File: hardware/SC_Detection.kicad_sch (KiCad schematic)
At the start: 86 parts, among them U15 LT1678CS8#PBF, U16 LT1678CS8#PBF, U17 LM211DRG4, U18 LM211DRG4, U19 LM211DRG4, U20 LM211DRG4

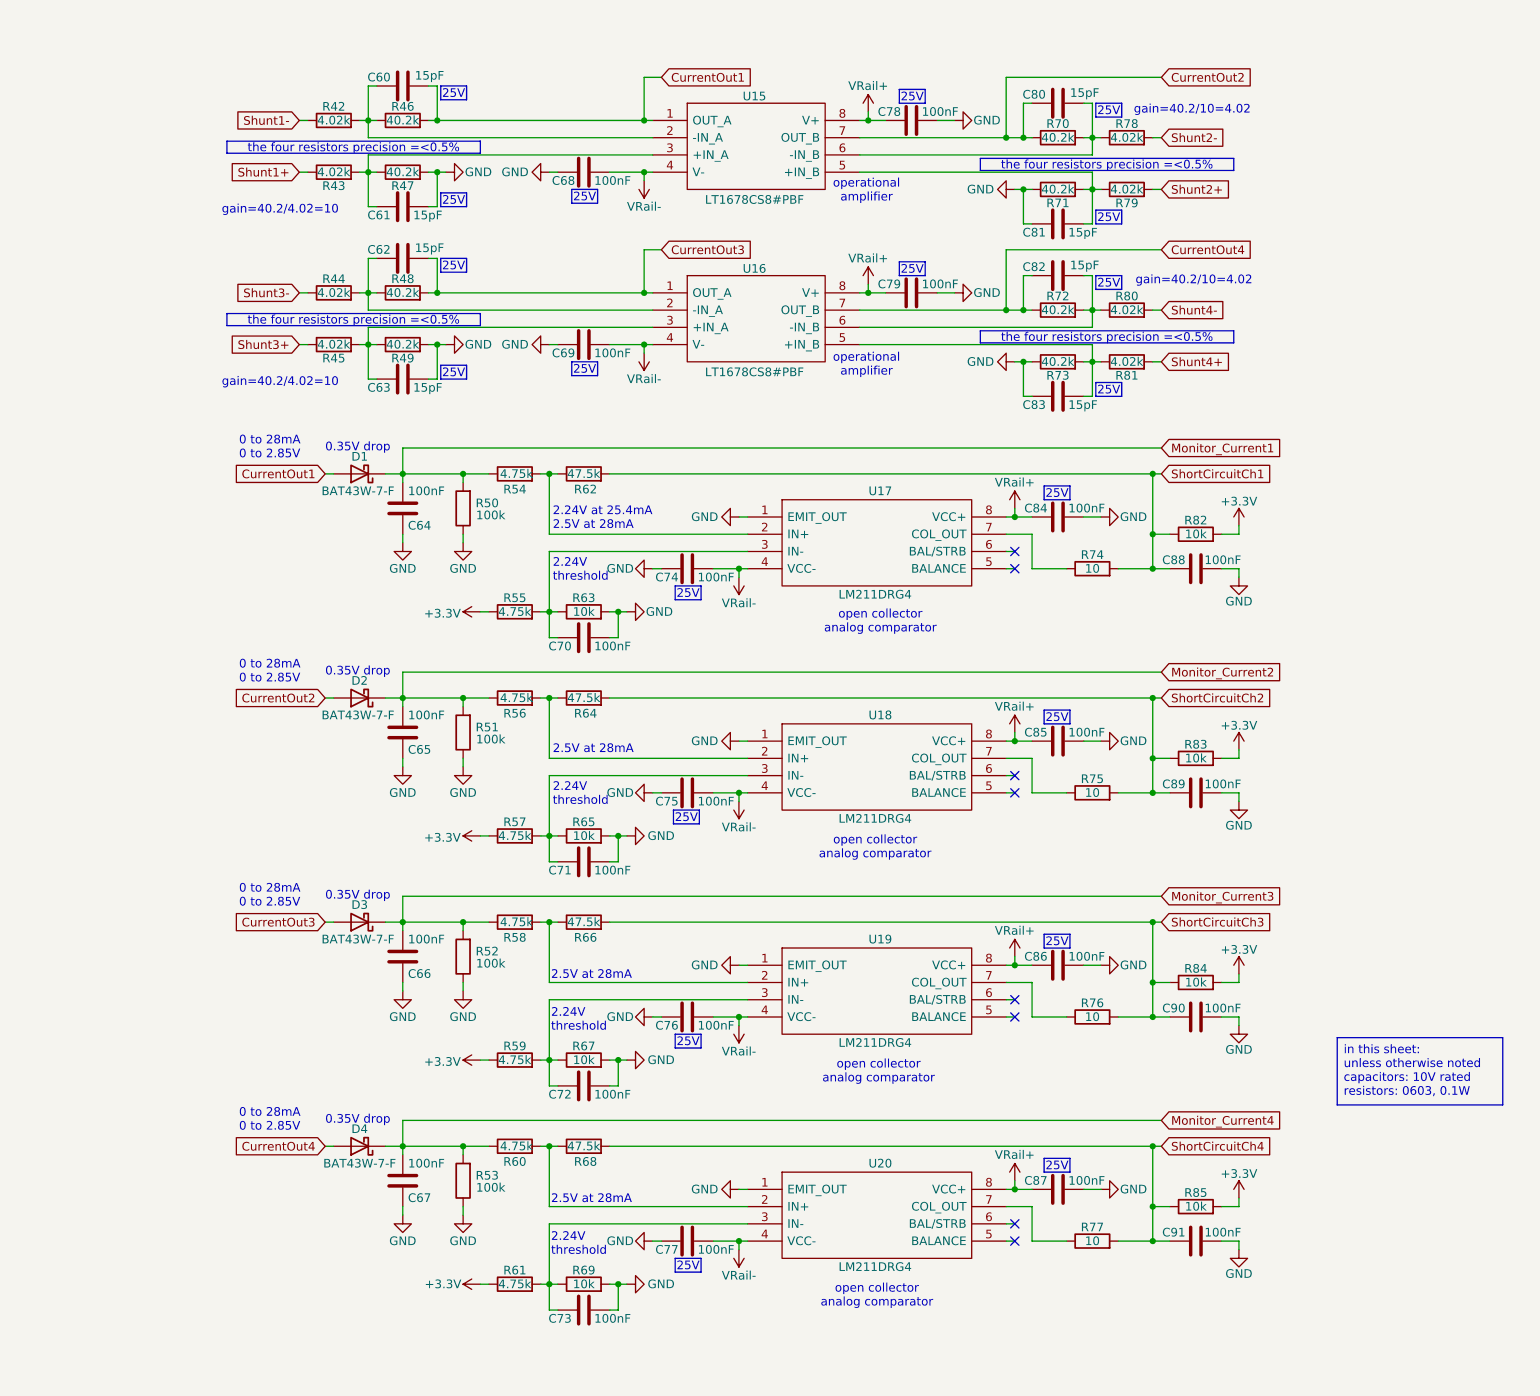
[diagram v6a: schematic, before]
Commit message: BOM for all capacitors and resistors is added correctly to the schematic
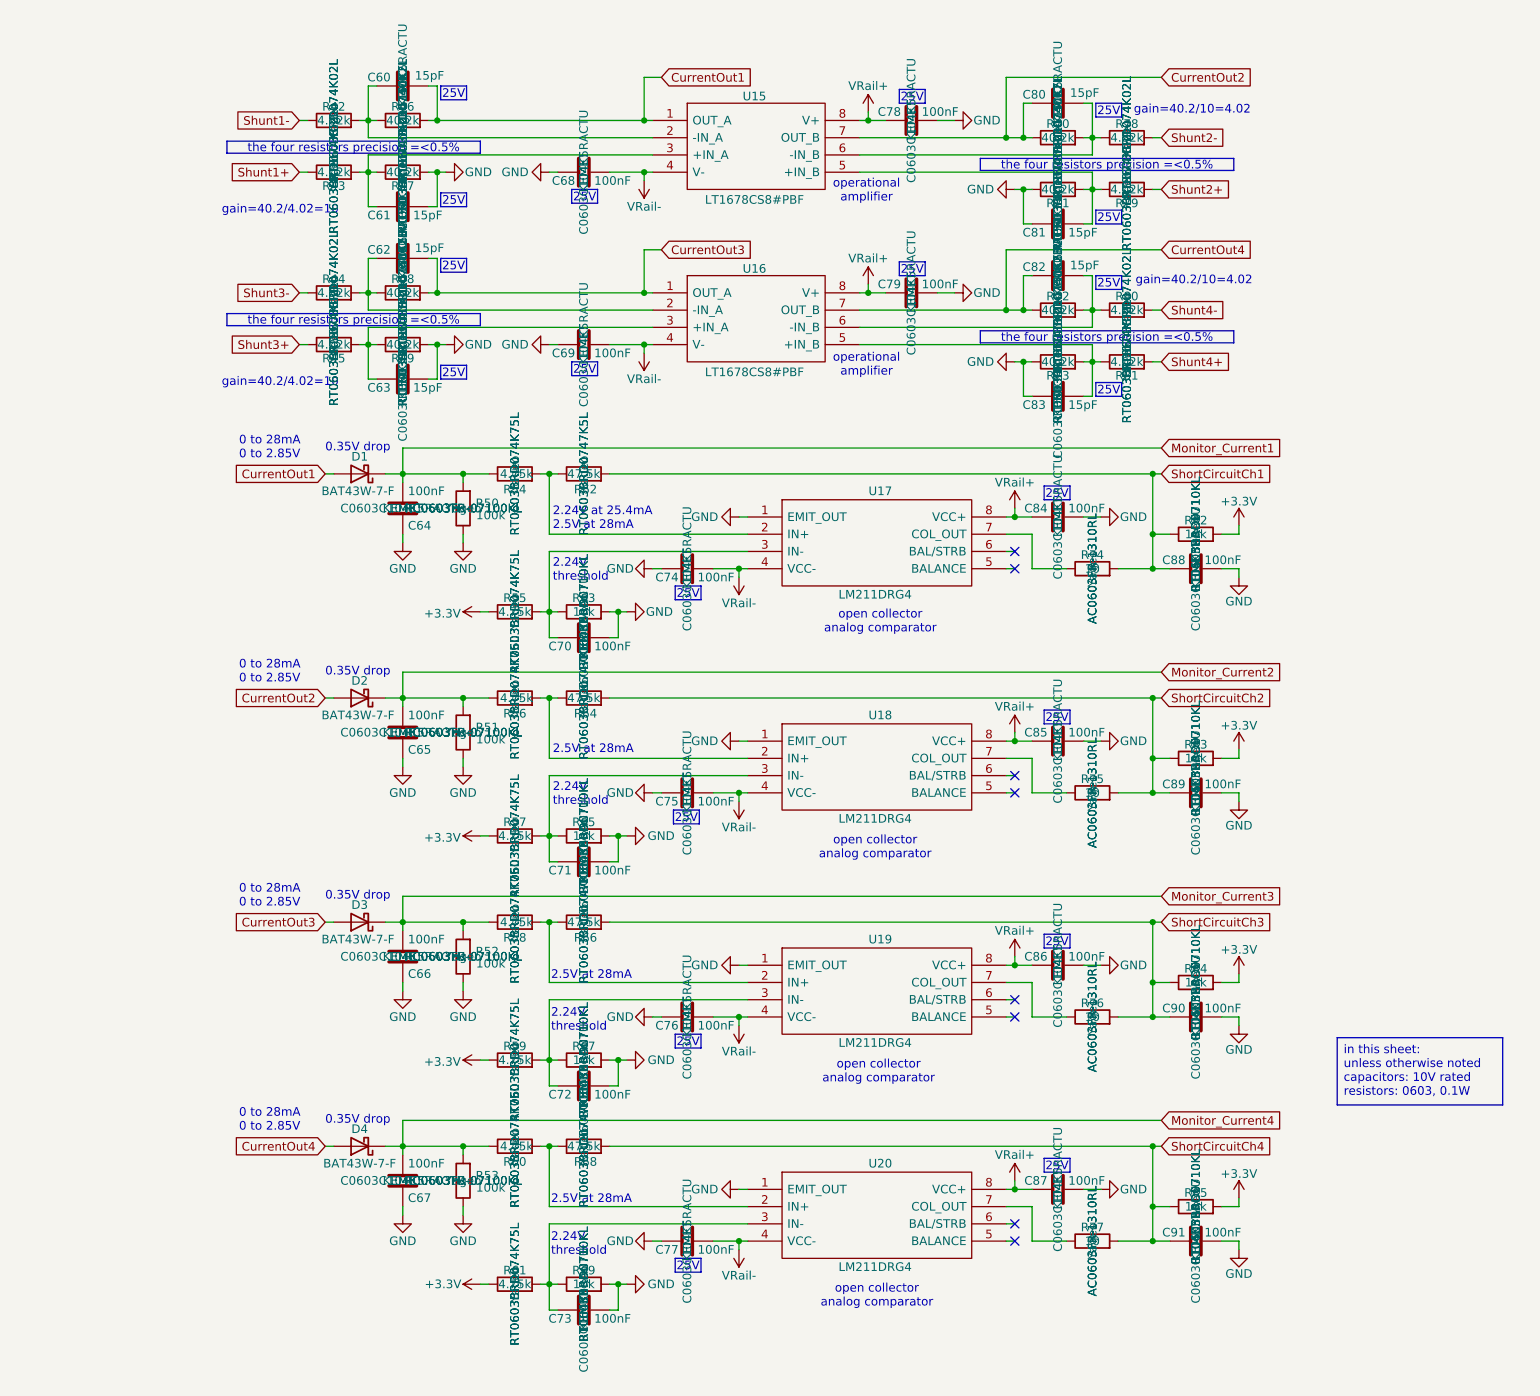
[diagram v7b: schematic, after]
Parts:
- C60, C61, C62, C63, C80, C81, C82, C83: Link https://www.digikey.com/en/products/detail/walsin-technolog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 -> https://www.digikey.com/en/products/detail/kemet/C0603C150K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; MPN (none) -> C0603C150K5RACTU; Manufacturer Walson Technology Corporation -> KEMET; Manufacturer Number 0402B104K160CT -> (none); Manufacturer_Name (none) -> KEMET; Manufacturer_Part_Number (none) -> C0603C150K5RACTU; Rated Voltage 16V -> 50V
- C64, C65, C66, C67, C68, C69, C70, C71, C72, C73, C74, C75, C76, C77, C78, C79, C84, C85, C86, C87, C88, C89, C90, C91: Link https://www.digikey.com/en/products/detail/walsin-technolog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 -> https://www.digikey.com/en/products/detail/kemet/C0603C104K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; MPN (none) -> C0603C104K5RACTU; Manufacturer Walson Technology Corporation -> KEMET; Manufacturer Number 0402B104K160CT -> (none); Manufacturer_Name (none) -> KEMET; Manufacturer_Part_Number (none) -> C0603C104K5RACTU; Rated Voltage 16V -> 50V
- R42, R43, R44, R45, R78, R79, R80, R81: Link https://www.digikey.com/en/products/detail/yageo/RT0402BRD0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 -> https://www.digikey.com/en/products/detail/yageo/RT0603BRD0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; MPN (none) -> RT0603BRD074K02L; Manufacturer_Name (none) -> Yageo; Manufacturer_Part_Number (none) -> RT0603BRD074K02L; Tolerance 1% -> 0.1%
- R46, R47, R48, R49, R70, R71, R72, R73: Link https://www.digikey.com/en/products/detail/yageo/RT0402BRD0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 -> https://www.digikey.com/en/products/detail/yageo/RT0603BRD0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; MPN (none) -> RT0603BRD0740K2L; Manufacturer_Name (none) -> Yageo; Manufacturer_Part_Number (none) -> RT0603BRD0740K2L; Tolerance 1% -> 0.1%
- R50, R51, R52, R53: Link https://www.digikey.com/en/products/detail/yageo/RT0402BRD0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 -> https://www.digikey.com/en/products/detail/yageo/RC0603FR-0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; MPN (none) -> RC0603FR-07100KL; Manufacturer_Name (none) -> Yageo; Manufacturer_Part_Number (none) -> RC0603FR-07100KL
- R54, R55, R56, R57, R58, R59, R60, R61: Link https://www.digikey.com/en/products/detail/yageo/RT0402BRD0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 -> https://www.digikey.com/en/products/detail/yageo/RT0603BRD0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; MPN (none) -> RT0603BRD074K75L; Manufacturer_Name (none) -> Yageo; Manufacturer_Part_Number (none) -> RT0603BRD074K75L; Tolerance 1% -> 0.1%
- R62, R64, R66, R68: Link https://www.digikey.com/en/products/detail/yageo/RT0402BRD0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 -> https://www.digikey.com/en/products/detail/yageo/RT0603BRD0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; MPN (none) -> RT0603BRD0747K5L; Manufacturer_Name (none) -> Yageo; Manufacturer_Part_Number (none) -> RT0603BRD0747K5L
- R63, R65, R67, R69, R82, R83, R84, R85: Link https://www.digikey.com/en/products/detail/yageo/RT0402BRD0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 -> https://www.digikey.com/en/products/detail/yageo/RT0603BRD0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; MPN (none) -> RT0603BRD0710KL; Manufacturer_Name (none) -> Yageo; Manufacturer_Part_Number (none) -> RT0603BRD0710KL; Tolerance 1% -> 0.1%
- R74, R75, R76, R77: Link https://www.digikey.com/en/products/detail/yageo/RT0402BRD0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 -> https://www.digikey.com/en/products/detail/yageo/AC0603FR-1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; MPN (none) -> AC0603FR-1310RL; Manufacturer_Name (none) -> Yageo; Manufacturer_Part_Number (none) -> AC0603FR-1310RL

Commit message: Not necessary text is hidden + BOM on schematic
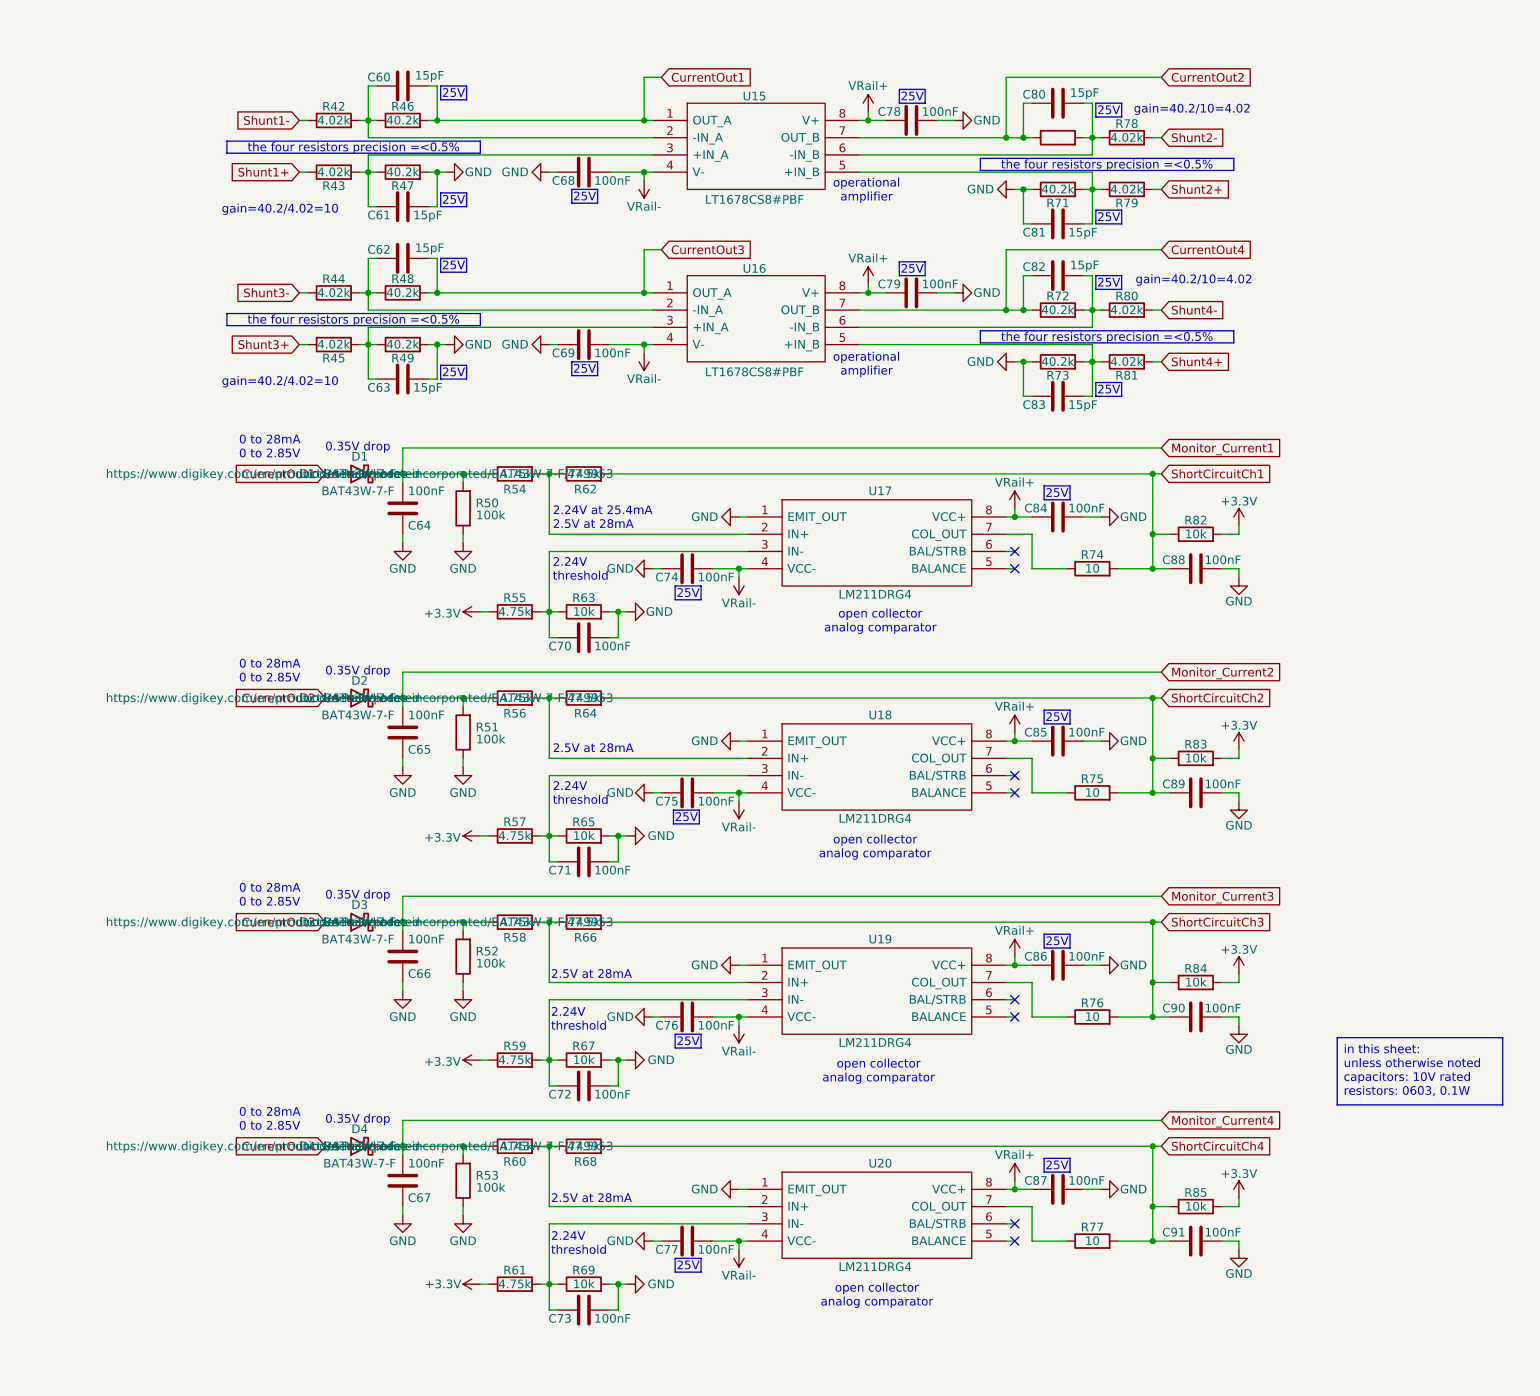
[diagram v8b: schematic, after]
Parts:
- C60, C61, C62, C63, C64, C65, C66, C67, C68, C69, C70, C71, C72, C73, C74, C75, C76, C77, C78, C79, C80, C81, C82, C83, C84, C85, C86, C87, C88, C89, C90, C91: Temperature Coefficient X7R -> (none)
- D1, D2, D3, D4: Link (none) -> https://www.digikey.com/en/products/detail/diodes-incorpora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; Manufacturer (none) -> Diodes Incorporated; Manufacturer_Part_Number (none) -> BAT43W-7-F
- R62, R64, R66, R68: Tolerance 1% -> 0.1%
- U15, U16: MPN (none) -> LT1678CS8#PBF
- U17, U18, U19, U20: MPN (none) -> LM211DRG4
